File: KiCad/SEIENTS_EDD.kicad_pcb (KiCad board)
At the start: 2 copper layers, 140 x 90 mm, 99 parts, among them IC1 A3144EUA, J1 Conn_01x02_Pin, J201 Screw_Terminal_01x04, J3 Screw_Terminal_01x05, J4 Screw_Terminal_01x02, J7 DE9_Socket, J8 DE9_Pins, M4 Motor_DC, M5 Motor_DC, M6 Motor_DC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

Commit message: Modificació al placement
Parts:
- moved J7 14.0 mm to (87.8, 89.3), turned to -90 degrees
- moved J8 12.6 mm to (87.7, 110.2), turned to -90 degrees
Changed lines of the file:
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@@
 	(footprint "Connector_Dsub:DSUB-9_Pins_Horizontal_P2.77x2.84mm_EdgePinOffset4.94mm_Housed_MountingHolesOffset4.94mm"
 		(layer "F.Cu")
-		(at 84.41 122.39 90)
+		(at 87.74 110.2 -90)
 		(descr "9-pin D-Sub connector, horizontal/angled (90 deg), THT-mount, pins (male), pitch 2.77x2.84mm, pin-PCB-offset 4.94mm, distance of mounting holes 25mm, distance of mounting holes to PCB edge 4.94mm, see https://disti-assets.s3.amazonaws.com/tonar/files/datasheets/16730.pdf")
 		(tags "9-pin D-Sub connector horizontal angled 90deg THT pins pitch 2.77x2.84mm pin-PCB-offset 4.94mm mounting-holes-distance 25mm mounting-hole-offset 4.94mm")
@@
 		(attr through_hole)
 		(fp_line
-			(start 0.25 -2.754338)
-			(end 0 -2.321325)
+			(start -9.945 7.72)
+			(end -9.945 -1.86)
 			(stroke
 				(width 0.12)
@@
 		)
 		(fp_line
-			(start -0.25 -2.754338)
-			(end 0.25 -2.754338)
+			(start -9.945 -1.86)
+			(end 21.025 -1.86)
 			(stroke
 				(width 0.12)
@@
 		)
 		(fp_line
-			(start 0 -2.321325)
-			(end -0.25 -2.754338)
+			(start 21.025 -1.86)
+			(end 21.025 7.72)
 			(stroke
 				(width 0.12)
@@
 		)
 		(fp_line
-			(start 21.025 -1.86)
-			(end 21.025 7.72)
+			(start 0 -2.321325)
+			(end -0.25 -2.754338)
 			(stroke
 				(width 0.12)
@@
 		)
 		(fp_line
-			(start -9.945 -1.86)
-			(end 21.025 -1.86)
+			(start -0.25 -2.754338)
+			(end 0.25 -2.754338)
 			(stroke
 				(width 0.12)
@@
 		)
 		(fp_line
-			(start -9.945 7.72)
-			(end -9.945 -1.86)
+			(start 0.25 -2.754338)
+			(end 0 -2.321325)
 			(stroke
 				(width 0.12)
@@
 		)
 		(fp_line
-			(start 19.64 7.78)
-			(end 19.64 2.84)
+			(start -8.56 7.78)
+			(end -8.56 2.84)
 			(stroke
 				(width 0.1)
@@
 		)
 		(fp_line
-			(start 16.44 7.78)
-			(end 16.44 2.84)
+			(start -5.36 7.78)
+			(end -5.36 2.84)
 			(stroke
 				(width 0.1)
@@
 		)
 		(fp_line
-			(start -5.36 7.78)
-			(end -5.36 2.84)
+			(start 16.44 7.78)
+			(end 16.44 2.84)
 			(stroke
 				(width 0.1)
@@
 		)
 		(fp_line
-			(start -8.56 7.78)
-			(end -8.56 2.84)
+			(start 19.64 7.78)
+			(end 19.64 2.84)
 			(stroke
 				(width 0.1)
@@
 		)
 		(fp_rect
-			(start -9.885 -1.8)
-			(end 20.965 7.78)
+			(start -9.46 8.18)
+			(end -4.46 13.18)
 			(stroke
 				(width 0.1)
@@
 		)
 		(fp_rect
-			(start -9.885 7.78)
-			(end 20.965 8.18)
+			(start -2.61 8.18)
+			(end 13.69 14.18)
 			(stroke
 				(width 0.1)
@@
 		)
 		(fp_rect
-			(start -2.61 8.18)
-			(end 13.69 14.18)
+			(start -9.885 7.78)
+			(end 20.965 8.18)
 			(stroke
 				(width 0.1)
@@
 		)
 		(fp_rect
-			(start -9.46 8.18)
-			(end -4.46 13.18)
+			(start -9.885 -1.8)
+			(end 20.965 7.78)
 			(stroke
 				(width 0.1)
@@
 		)
 		(fp_arc
-			(start 16.44 2.84)
-			(mid 18.04 1.24)
-			(end 19.64 2.84)
+			(start -8.56 2.84)
+			(mid -6.96 1.24)
+			(end -5.36 2.84)
 			(stroke
 				(width 0.1)
@@
 		)
 		(fp_arc
-			(start -8.56 2.84)
-			(mid -6.96 1.24)
-			(end -5.36 2.84)
+			(start 16.44 2.84)
+			(mid 18.04 1.24)
+			(end 19.64 2.84)
 			(stroke
 				(width 0.1)
@@
 		)
 		(pad "0" thru_hole circle
-			(at -6.96 2.84 90)
+			(at -6.96 2.84 270)
 			(size 4 4)
 			(drill 3.2)
@@
 		)
 		(pad "0" thru_hole circle
-			(at 18.04 2.84 90)
+			(at 18.04 2.84 270)
 			(size 4 4)
 			(drill 3.2)
@@
 		)
 		(pad "1" thru_hole rect
-			(at 0 0 90)
+			(at 0 0 270)
 			(size 1.6 1.6)
 			(drill 1)
@@
 		)
 		(pad "2" thru_hole circle
-			(at 2.77 0 90)
+			(at 2.77 0 270)
 			(size 1.6 1.6)
 			(drill 1)
@@
 		)
 		(pad "3" thru_hole circle
-			(at 5.54 0 90)
+			(at 5.54 0 270)
 			(size 1.6 1.6)
 			(drill 1)
@@
 		)
 		(pad "4" thru_hole circle
-			(at 8.31 0 90)
+			(at 8.31 0 270)
 			(size 1.6 1.6)
 			(drill 1)
@@
 		)
 		(pad "5" thru_hole circle
-			(at 11.08 0 90)
+			(at 11.08 0 270)
 			(size 1.6 1.6)
 			(drill 1)
@@
 		)
 		(pad "6" thru_hole circle
-			(at 1.385 2.84 90)
+			(at 1.385 2.84 270)
 			(size 1.6 1.6)
 			(drill 1)
@@
 		)
 		(pad "7" thru_hole circle
-			(at 4.155 2.84 90)
+			(at 4.155 2.84 270)
 			(size 1.6 1.6)
 			(drill 1)
@@
 		)
 		(pad "8" thru_hole circle
-			(at 6.925 2.84 90)
+			(at 6.925 2.84 270)
 			(size 1.6 1.6)
 			(drill 1)
@@
 		)
 		(pad "9" thru_hole circle
-			(at 9.695 2.84 90)
+			(at 9.695 2.84 270)
 			(size 1.6 1.6)
 			(drill 1)
@@
 	(footprint "Connector_Dsub:DSUB-9_Socket_Horizontal_P2.77x2.84mm_EdgePinOffset4.94mm_Housed_MountingHolesOffset4.94mm"
 		(layer "F.Cu")
-		(at 84.56 75.71 90)
+		(at 87.84 89.28 -90)
 		(descr "9-pin D-Sub connector, horizontal/angled (90 deg), THT-mount, socket (female), pitch 2.77x2.84mm, pin-PCB-offset 4.94mm, distance of mounting holes 25mm, distance of mounting holes to PCB edge 4.94mm, see https://disti-assets.s3.amazonaws.com/tonar/files/datasheets/16730.pdf")
 		(tags "9-pin D-Sub connector horizontal angled 90deg THT socket pitch 2.77x2.84mm pin-PCB-offset 4.94mm mounting-holes-distance 25mm mounting-hole-offset 4.94mm")
@@
 		(attr through_hole)
 		(fp_line
-			(start 0.25 -2.754338)
-			(end 0 -2.321325)
+			(start -21.025 7.72)
+			(end -21.025 -1.86)
 			(stroke
 				(width 0.12)
@@
 		)
 		(fp_line
-			(start -0.25 -2.754338)
-			(end 0.25 -2.754338)
+			(start -21.025 -1.86)
+			(end 9.945 -1.86)
 			(stroke
 				(width 0.12)
@@
 		)
 		(fp_line
-			(start 0 -2.321325)
-			(end -0.25 -2.754338)
+			(start 9.945 -1.86)
+			(end 9.945 7.72)
 			(stroke
 				(width 0.12)
@@
 		)
 		(fp_line
-			(start 9.945 -1.86)
-			(end 9.945 7.72)
+			(start 0 -2.321325)
+			(end -0.25 -2.754338)
 			(stroke
 				(width 0.12)
@@
 		)
 		(fp_line
-			(start -21.025 -1.86)
-			(end 9.945 -1.86)
+			(start -0.25 -2.754338)
+			(end 0.25 -2.754338)
 			(stroke
 				(width 0.12)
@@
 		)
 		(fp_line
-			(start -21.025 7.72)
-			(end -21.025 -1.86)
+			(start 0.25 -2.754338)
+			(end 0 -2.321325)
 			(stroke
 				(width 0.12)
@@
 		)
 		(fp_line
-			(start 8.56 7.78)
-			(end 8.56 2.84)
+			(start -19.64 7.78)
+			(end -19.64 2.84)
 			(stroke
 				(width 0.1)
@@
 		)
 		(fp_line
-			(start 5.36 7.78)
-			(end 5.36 2.84)
+			(start -16.44 7.78)
+			(end -16.44 2.84)
 			(stroke
 				(width 0.1)
@@
 		)
 		(fp_line
-			(start -16.44 7.78)
-			(end -16.44 2.84)
+			(start 5.36 7.78)
+			(end 5.36 2.84)
 			(stroke
 				(width 0.1)
@@
 		)
 		(fp_line
-			(start -19.64 7.78)
-			(end -19.64 2.84)
+			(start 8.56 7.78)
+			(end 8.56 2.84)
 			(stroke
 				(width 0.1)
@@
 		)
 		(fp_rect
-			(start -20.965 -1.8)
-			(end 9.885 7.78)
+			(start -20.54 8.18)
+			(end -15.54 13.18)
 			(stroke
 				(width 0.1)
@@
 		)
 		(fp_rect
-			(start -20.965 7.78)
-			(end 9.885 8.18)
+			(start -13.69 8.18)
+			(end 2.61 14.35)
 			(stroke
 				(width 0.1)
@@
 		)
 		(fp_rect
-			(start -13.69 8.18)
-			(end 2.61 14.35)
+			(start -20.965 7.78)
+			(end 9.885 8.18)
 			(stroke
 				(width 0.1)
@@
 		)
 		(fp_rect
-			(start -20.54 8.18)
-			(end -15.54 13.18)
+			(start -20.965 -1.8)
+			(end 9.885 7.78)
 			(stroke
 				(width 0.1)
@@
 		)
 		(fp_arc
-			(start 5.36 2.84)
-			(mid 6.96 1.24)
-			(end 8.56 2.84)
+			(start -19.64 2.84)
+			(mid -18.04 1.24)
+			(end -16.44 2.84)
 			(stroke
 				(width 0.1)
@@
 		)
 		(fp_arc
-			(start -19.64 2.84)
-			(mid -18.04 1.24)
-			(end -16.44 2.84)
+			(start 5.36 2.84)
+			(mid 6.96 1.24)
+			(end 8.56 2.84)
 			(stroke
 				(width 0.1)
@@
 		)
 		(pad "0" thru_hole circle
-			(at -18.04 2.84 90)
+			(at -18.04 2.84 270)
 			(size 4 4)
 			(drill 3.2)
@@
 		)
 		(pad "0" thru_hole circle
-			(at 6.96 2.84 90)
+			(at 6.96 2.84 270)
 			(size 4 4)
 			(drill 3.2)
@@
 		)
 		(pad "1" thru_hole rect
-			(at 0 0 90)
+			(at 0 0 270)
 			(size 1.6 1.6)
 			(drill 1)
@@
 		)
 		(pad "2" thru_hole circle
-			(at -2.77 0 90)
+			(at -2.77 0 270)
 			(size 1.6 1.6)
 			(drill 1)
@@
 		)
 		(pad "3" thru_hole circle
-			(at -5.54 0 90)
+			(at -5.54 0 270)
 			(size 1.6 1.6)
 			(drill 1)
@@
 		)
 		(pad "4" thru_hole circle
-			(at -8.31 0 90)
+			(at -8.31 0 270)
 			(size 1.6 1.6)
 			(drill 1)
@@
 		)
 		(pad "5" thru_hole circle
-			(at -11.08 0 90)
+			(at -11.08 0 270)
 			(size 1.6 1.6)
 			(drill 1)
@@
 		)
 		(pad "6" thru_hole circle
-			(at -1.385 2.84 90)
+			(at -1.385 2.84 270)
 			(size 1.6 1.6)
 			(drill 1)
@@
 		)
 		(pad "7" thru_hole circle
-			(at -4.155 2.84 90)
+			(at -4.155 2.84 270)
 			(size 1.6 1.6)
 			(drill 1)
@@
 		)
 		(pad "8" thru_hole circle
-			(at -6.925 2.84 90)
+			(at -6.925 2.84 270)
 			(size 1.6 1.6)
 			(drill 1)
@@
 		)
 		(pad "9" thru_hole circle
-			(at -9.695 2.84 90)
+			(at -9.695 2.84 270)
 			(size 1.6 1.6)
 			(drill 1)

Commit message: Placement inicial acabat
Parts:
- moved SW9 271.0 mm to (147.5, 113.8), turned to -90 degrees
- moved SW10 265.1 mm to (143.1, 113.8), turned to -90 degrees
- moved SW11 259.1 mm to (138.6, 113.8), turned to -90 degrees
- moved R16 254.2 mm to (143.5, 120.2), turned to -90 degrees
- moved SW12 253.2 mm to (134.2, 113.8), turned to -90 degrees
- moved R17 250.3 mm to (140.6, 120.2), turned to -90 degrees
- moved SW13 247.3 mm to (129.7, 113.8), turned to -90 degrees
- moved R18 246.5 mm to (137.6, 120.2), turned to -90 degrees
- moved C9 246.3 mm to (188.8, 71.1)
- moved R19 242.6 mm to (134.7, 120.2), turned to -90 degrees
- moved SW14 241.5 mm to (125.2, 113.8), turned to -90 degrees
- moved R20 238.8 mm to (131.7, 120.2), turned to -90 degrees
- moved SW15 235.6 mm to (120.8, 113.8), turned to -90 degrees
- moved R21 235.0 mm to (128.8, 120.2), turned to -90 degrees
- moved C26 231.9 mm to (111.7, 122.6), turned to 90 degrees
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
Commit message: Modificació al placement
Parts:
- moved REF** 10.3 mm to (94.7, 59.5)
- moved J7 10.2 mm to (98.0, 89.3)
- moved J8 10.2 mm to (97.9, 110.3)
- moved REF** 9.90 mm to (94.7, 140.3)
- moved C27 9.57 mm to (115.9, 89.8), turned to 90 degrees
- moved C26 9.42 mm to (120.1, 126.9)
- moved R15 9.42 mm to (108.9, 127.0)
- moved U3 9.42 mm to (114.4, 127.0)
- moved C12 9.42 mm to (111.5, 122.1)
- moved R4 7.94 mm to (116.0, 96.6)
- moved R2 5.91 mm to (116.0, 104.4)
- moved C25 5.86 mm to (115.9, 78.4)
- moved C13 4.46 mm to (115.8, 84.0)
- moved C20 3.94 mm to (104.3, 87.6)
- moved C28 3.94 mm to (104.2, 83.4)
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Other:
- board size 140 x 90 mm -> 130.1 x 90 mm

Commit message: Modificació al placement
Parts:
- moved C25 1.93 mm to (117.5, 79.5)
- moved C13 1.60 mm to (117.3, 84.4), turned to 180 degrees
- moved C27 1.46 mm to (117.3, 89.6), turned to 0 degrees
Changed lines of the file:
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@@
 	(footprint "Capacitor_SMD:C_0805_2012Metric"
 		(layer "F.Cu")
-		(at 115.9 78.4 90)
+		(at 117.45 79.55 90)
 		(descr "Capacitor SMD 0805 (2012 Metric), square (rectangular) end terminal, IPC-7351 nominal, (Body size source: IPC-SM-782 page 76, https://www.pcb-3d.com/wordpress/wp-content/uploads/ipc-sm-782a_amendment_1_and_2.pdf, https://docs.google.com/spreadsheets/d/1BsfQQcO9C6DZCsRaXUlFlo91Tg2WpOkGARC1WS5S8t0/edit?usp=sharing), generated with kicad-footprint-generator")
 		(tags "capacitor")
@@
 	(footprint "Capacitor_SMD:C_0805_2012Metric"
 		(layer "F.Cu")
-		(at 115.8 84 90)
+		(at 117.35 84.4 180)
 		(descr "Capacitor SMD 0805 (2012 Metric), square (rectangular) end terminal, IPC-7351 nominal, (Body size source: IPC-SM-782 page 76, https://www.pcb-3d.com/wordpress/wp-content/uploads/ipc-sm-782a_amendment_1_and_2.pdf, https://docs.google.com/spreadsheets/d/1BsfQQcO9C6DZCsRaXUlFlo91Tg2WpOkGARC1WS5S8t0/edit?usp=sharing), generated with kicad-footprint-generator")
 		(tags "capacitor")
 		(property "Reference" "C13"
-			(at 0 -1.68 90)
+			(at 0 -1.68 0)
 			(layer "F.SilkS")
 			(effects
@@
 		)
 		(property "Value" "100 nF"
-			(at 0 1.68 90)
+			(at 0 1.68 0)
 			(layer "F.Fab")
 			(effects
@@
 		)
 		(property "Datasheet" "~"
-			(at 0 0 90)
+			(at 0 0 0)
 			(layer "F.Fab")
 			(hide yes)
@@
 		)
 		(property "Description" "Unpolarized capacitor"
-			(at 0 0 90)
+			(at 0 0 0)
 			(layer "F.Fab")
 			(hide yes)
@@
 		(attr smd)
 		(fp_line
-			(start -0.261252 -0.735)
-			(end 0.261252 -0.735)
+			(start -0.261252 0.735)
+			(end 0.261252 0.735)
 			(stroke
 				(width 0.12)
@@
 		)
 		(fp_line
-			(start -0.261252 0.735)
-			(end 0.261252 0.735)
+			(start -0.261252 -0.735)
+			(end 0.261252 -0.735)
 			(stroke
 				(width 0.12)
@@
 		)
 		(fp_text user "${REFERENCE}"
-			(at 0 0 90)
+			(at 0 0 0)
 			(layer "F.Fab")
 			(effects
@@
 		)
 		(pad "1" smd roundrect
-			(at -0.95 0 90)
+			(at -0.95 0 180)
 			(size 1 1.45)
 			(layers "F.Cu" "F.Mask" "F.Paste")
@@
 		)
 		(pad "2" smd roundrect
-			(at 0.95 0 90)
+			(at 0.95 0 180)
 			(size 1 1.45)
 			(layers "F.Cu" "F.Mask" "F.Paste")
@@
 	(footprint "Capacitor_SMD:C_0805_2012Metric"
 		(layer "F.Cu")
-		(at 115.9 89.8 90)
+		(at 117.35 89.6)
 		(descr "Capacitor SMD 0805 (2012 Metric), square (rectangular) end terminal, IPC-7351 nominal, (Body size source: IPC-SM-782 page 76, https://www.pcb-3d.com/wordpress/wp-content/uploads/ipc-sm-782a_amendment_1_and_2.pdf, https://docs.google.com/spreadsheets/d/1BsfQQcO9C6DZCsRaXUlFlo91Tg2WpOkGARC1WS5S8t0/edit?usp=sharing), generated with kicad-footprint-generator")
 		(tags "capacitor")
 		(property "Reference" "C27"
-			(at 0 -1.68 90)
+			(at 0 -1.68 0)
 			(layer "F.SilkS")
 			(effects
@@
 		)
 		(property "Value" "100 nF"
-			(at 0 1.68 90)
+			(at 0 1.68 0)
 			(layer "F.Fab")
 			(effects
@@
 		)
 		(property "Datasheet" "~"
-			(at 0 0 90)
+			(at 0 0 0)
 			(layer "F.Fab")
 			(hide yes)
@@
 		)
 		(property "Description" "Unpolarized capacitor"
-			(at 0 0 90)
+			(at 0 0 0)
 			(layer "F.Fab")
 			(hide yes)
@@
 		)
 		(fp_text user "${REFERENCE}"
-			(at 0 0 90)
+			(at 0 0 0)
 			(layer "F.Fab")
 			(effects
@@
 		)
 		(pad "1" smd roundrect
-			(at -0.95 0 90)
+			(at -0.95 0)
 			(size 1 1.45)
 			(layers "F.Cu" "F.Mask" "F.Paste")
@@
 		)
 		(pad "2" smd roundrect
-			(at 0.95 0 90)
+			(at 0.95 0)
 			(size 1 1.45)
 			(layers "F.Cu" "F.Mask" "F.Paste")

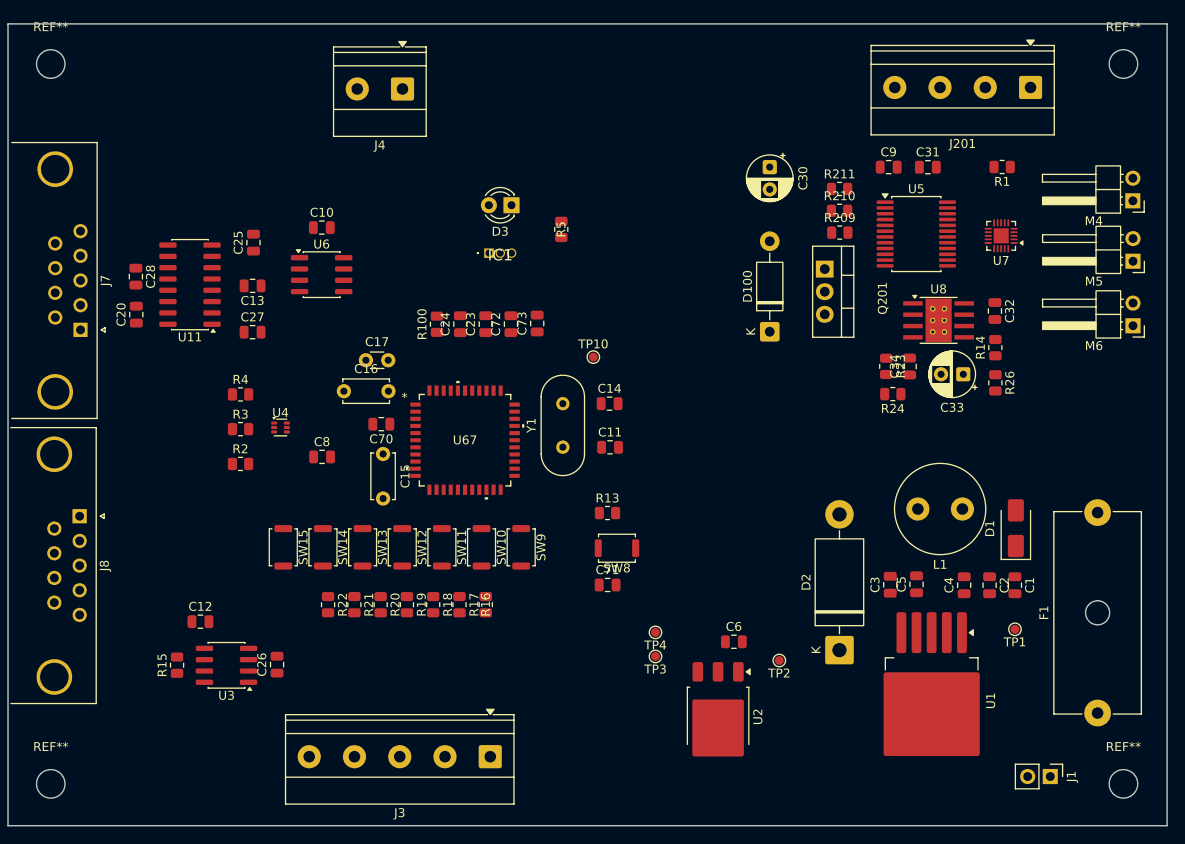
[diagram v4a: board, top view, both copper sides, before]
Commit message: Modificació Placement
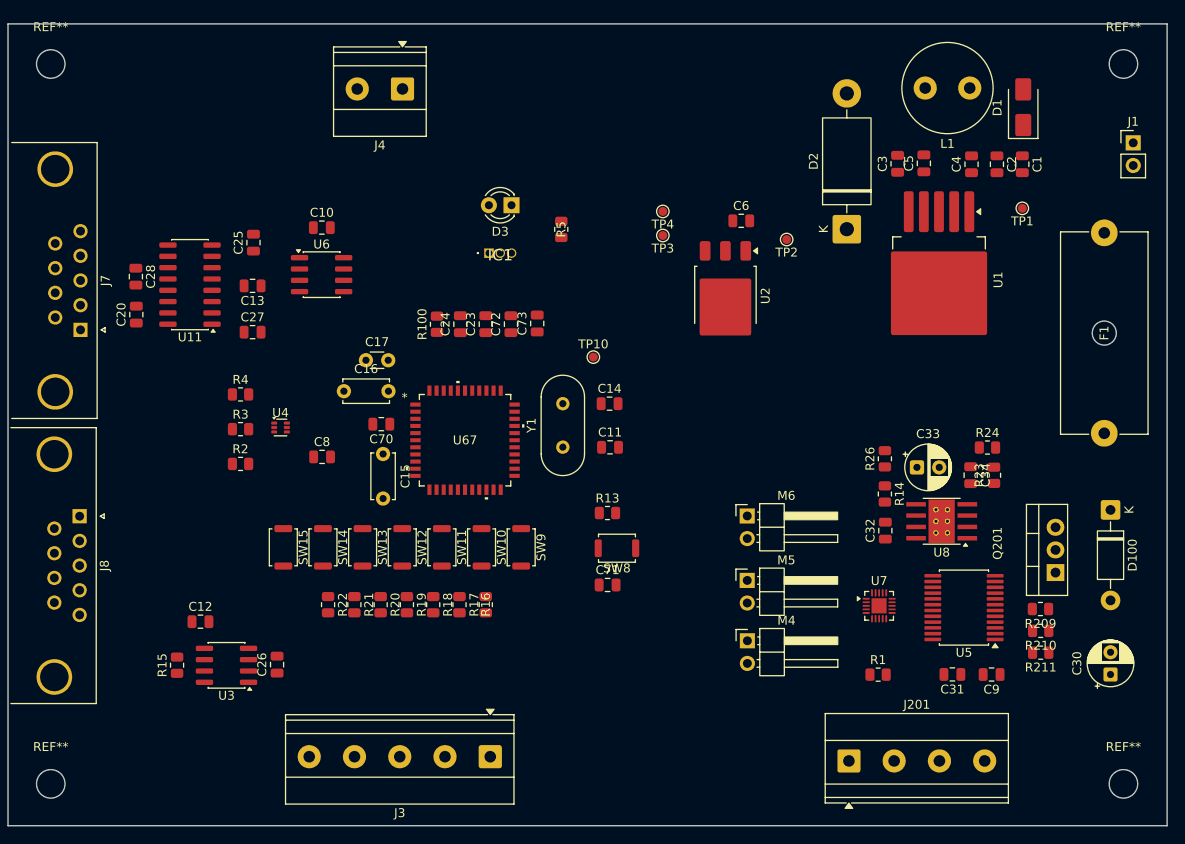
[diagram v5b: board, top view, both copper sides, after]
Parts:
- moved J201 78.3 mm to (184.3, 137.7), turned to 0 degrees
- moved J1 71.7 mm to (216.2, 68.3), turned to 0 degrees
- moved C30 68.6 mm to (213.7, 128.0), turned to 90 degrees
- moved M4 65.7 mm to (172.9, 124.2), turned to 0 degrees
- moved R1 58.7 mm to (187.6, 128.0), turned to 0 degrees
- moved C9 58.1 mm to (200.3, 128.0), turned to 180 degrees
- moved C31 57.0 mm to (195.9, 128.0), turned to 180 degrees
- moved R211 56.7 mm to (205.8, 125.6), turned to 180 degrees
- moved M5 56.2 mm to (172.9, 117.5), turned to 0 degrees
- moved R210 52.3 mm to (205.8, 123.1), turned to 180 degrees
- moved M6 48.3 mm to (172.9, 110.2), turned to 0 degrees
- moved R209 47.9 mm to (205.8, 120.7), turned to 180 degrees
- moved C1 47.3 mm to (203.8, 70.8)
- moved C2 47.3 mm to (200.9, 70.8)
- moved C3 47.3 mm to (189.8, 70.7)
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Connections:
- J7 pad 4: unconnected-(J7-Pad4) -> +3.3V
- J7 pad 9: unconnected-(J7-Pad9) -> +5V
- J8 pad 6: unconnected-(J8-Pad6) -> +5V
- J8 pad 8: unconnected-(J8-Pad8) -> +3.3V

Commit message: Modificacio
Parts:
- moved M6 46.4 mm to (216.0, 127.3), turned to 180 degrees
- moved M4 44.5 mm to (216.0, 113.3), turned to 180 degrees
- moved M5 43.2 mm to (216.0, 120.0), turned to 180 degrees
- moved C30 33.7 mm to (179.9, 128.5)
- moved D100 33.7 mm to (179.9, 110.0)
- moved Q201 33.7 mm to (173.8, 117.1)
- moved R209 33.7 mm to (172.1, 121.2)
- moved R210 33.7 mm to (172.1, 123.6)
- moved R211 33.7 mm to (172.1, 126.0)
